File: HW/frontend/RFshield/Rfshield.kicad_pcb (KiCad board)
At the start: 4 copper layers, 73 x 50.9 mm, 432 parts, among them P1 CONN_01X01, P38 CLKIN, P39 CLKOUT, Q1 MOSFET_P, T1 RX_BALUN, T2 TX_BALUN, U1 MAX2837, U2 MAX5864, U3 SI5351C, X1 GSG-XTAL4PIN

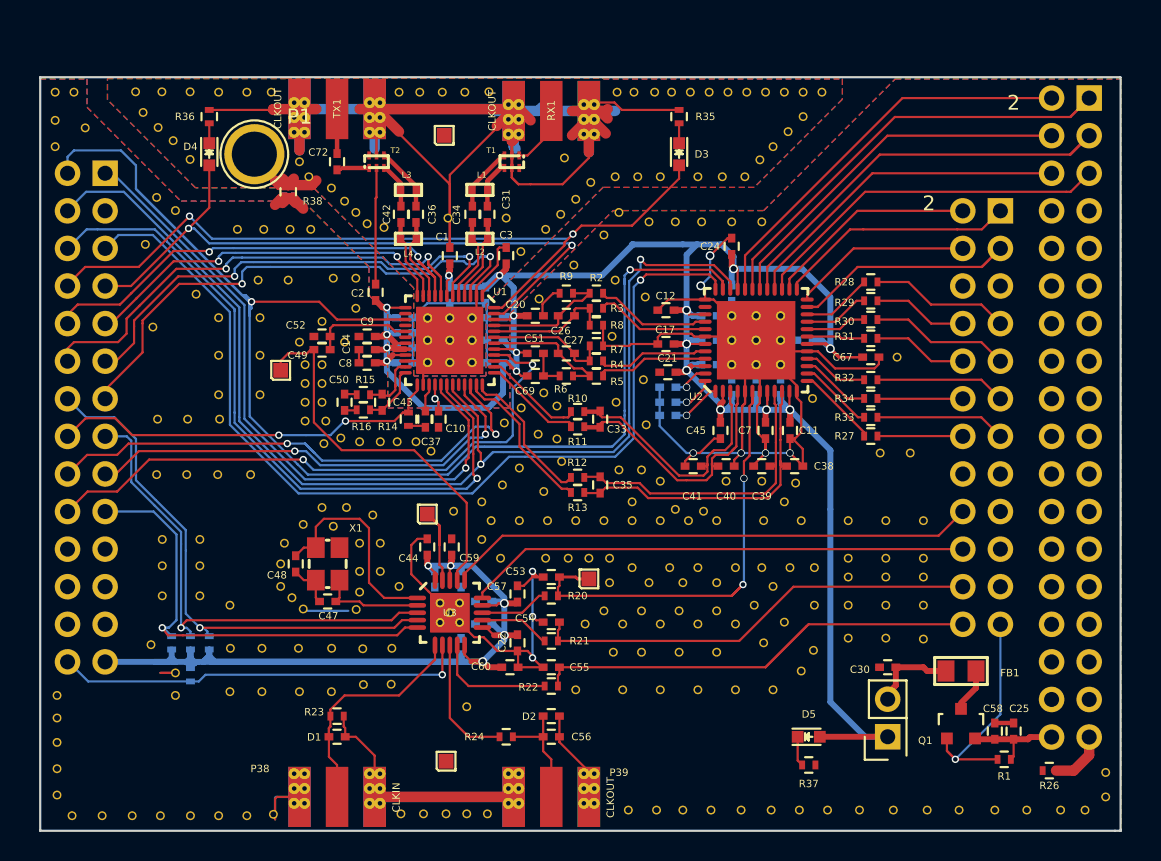
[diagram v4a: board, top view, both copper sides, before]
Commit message: Final text corrections
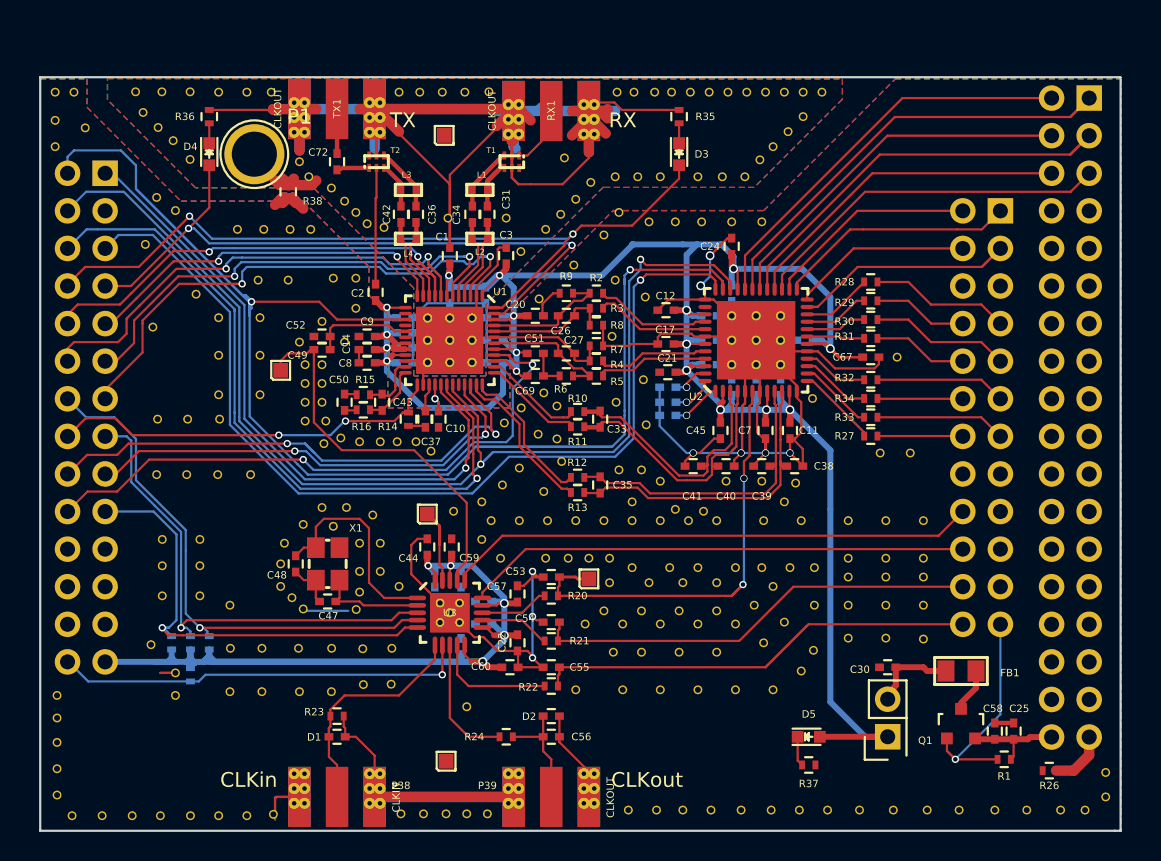
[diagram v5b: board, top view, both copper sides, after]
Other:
- board text added: "CLKin"
- board text added: "CLKout"
- board text added: "Quacho RF Shield v 1.0"
- board text added: "RX"
- board text added: "TX"
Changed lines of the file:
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@@
-(kicad_pcb (version 4) (host pcbnew 4.0.2-stable)
+(kicad_pcb (version 4) (host pcbnew 4.0.0-rc1-stable)
   (general
     (links 723)
     (no_connects 26)
-    (area 12.754 47.4758 123.009 132.4832)
+    (area 12.754 47.4758 122.5645 132.4832)
     (thickness 1.6)
-    (drawings 8)
+    (drawings 13)
     (tracks 1547)
     (zones 0)
@@
     (34 B.Paste user hide)
     (35 F.Paste user)
-    (36 B.SilkS user hide)
+    (36 B.SilkS user)
     (37 F.SilkS user)
     (38 B.Mask user hide)
@@
     (pad_to_mask_clearance 0)
     (aux_axis_origin 20 90)
-    (visible_elements 7FFECA3F)
+    (visible_elements 7FFEFFFF)
     (pcbplotparams
       (layerselection 0x010fc_80000001)
@@
   (module hackrf1:GSG-SMA-EDGE (layer F.Cu)
     (at 40.386 117.856 90)
-    (fp_text reference P38 (at 3.937 -5.207 180) (layer F.SilkS)
+    (fp_text reference P38 (at 2.794 4.318 180) (layer F.SilkS)
       (effects (font (size 0.50038 0.50038) (thickness 0.12446)))
     )
@@
   (module hackrf1:GSG-SMA-EDGE (layer F.Cu)
     (at 54.864 117.856 90)
-    (fp_text reference P39 (at 3.683 4.572 180) (layer F.SilkS)
+    (fp_text reference P39 (at 2.794 -4.318 180) (layer F.SilkS)
       (effects (font (size 0.50038 0.50038) (thickness 0.12446)))
     )
@@
       (net 94 0V_dig) (die_length -2147.483648))
   )
+  (gr_text TX (at 44.831 70.104) (layer F.SilkS)
+    (effects (font (size 1 1) (thickness 0.2)))
+  )
+  (gr_text RX (at 59.69 70.104) (layer F.SilkS)
+    (effects (font (size 1 1) (thickness 0.2)))
+  )
+  (gr_text CLKout (at 61.341 114.681) (layer F.SilkS)
+    (effects (font (size 1 1) (thickness 0.2)))
+  )
+  (gr_text CLKin (at 34.417 114.681) (layer F.SilkS)
+    (effects (font (size 1 1) (thickness 0.2)))
+  )
+  (gr_text "Quacho \nRF Shield\nv 1.0" (at 63.881 109.601) (layer B.SilkS)
+    (effects (font (size 2 2) (thickness 0.2)) (justify mirror))
+  )
   (gr_line (start 92.966 118.109) (end 93.336 118.109) (angle 90) (layer Edge.Cuts) (width 0.15))
   (gr_line (start 20.326 118.109) (end 92.966 118.109) (angle 90) (layer Edge.Cuts) (width 0.15))
@@
   (gr_line (start 20.326 67.209) (end 20.326 118.109) (angle 90) (layer Edge.Cuts) (width 0.15))
   (gr_line (start 20.316 67.189) (end 93.316 67.189) (angle 90) (layer Edge.Cuts) (width 0.15))
-  (gr_text 2 (at 86.103 68.919) (layer F.SilkS)
-    (effects (font (size 1 1) (thickness 0.25)))
+  (gr_text 2 (at 86.103 68.919) (layer B.SilkS)
+    (effects (font (size 1 1) (thickness 0.25)) (justify mirror))
   )
-  (gr_text 2 (at 80.383 75.719) (layer F.SilkS)
-    (effects (font (size 1 1) (thickness 0.25)))
+  (gr_text 2 (at 80.383 75.719) (layer B.SilkS)
+    (effects (font (size 1 1) (thickness 0.25)) (justify mirror))
   )
   (segment (start 91.213 88.919) (end 91.213 88.546) (width 0.15) (layer F.Cu) (net 0))
@@
   (segment (start 91.213 111.779) (end 91.213 113.003) (width 0.7) (layer F.Cu) (net 61))
   (segment (start 91.223 111.789) (end 91.213 111.779) (width 0.15) (layer F.Cu) (net 61))
-  (segment (start 85.213 104.159) (end 85.213 110.24) (width 0.15) (layer B.Cu) (net 62) (status 400000))
+  (segment (start 85.213 104.159) (end 85.213 110.24) (width 0.15) (layer B.Cu) (net 62))
   (segment (start 85.213 110.24) (end 82.169 113.284) (width 0.15) (layer B.Cu) (net 62))
   (segment (start 81.6 112.715) (end 82.169 113.284) (width 0.15) (layer F.Cu) (net 62))
@@
   (segment (start 44.45 79.502) (end 44.45 79.3115) (width 0.15) (layer F.Cu) (net 82))
   (segment (start 45.806 80.858) (end 44.45 79.502) (width 0.15) (layer F.Cu) (net 82))
-  (segment (start 36.576 86.995) (end 36.576 86.36) (width 0.15) (layer F.Cu) (net 83) (status 400000))
+  (segment (start 36.576 86.995) (end 36.576 86.36) (width 0.15) (layer F.Cu) (net 83))
   (segment (start 38.354 85.852) (end 37.084 85.852) (width 0.15) (layer F.Cu) (net 83))
   (segment (start 37.084 85.852) (end 36.576 86.36) (width 0.15) (layer F.Cu) (net 83))

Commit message: minor modifications
margin, vias and drc corrections
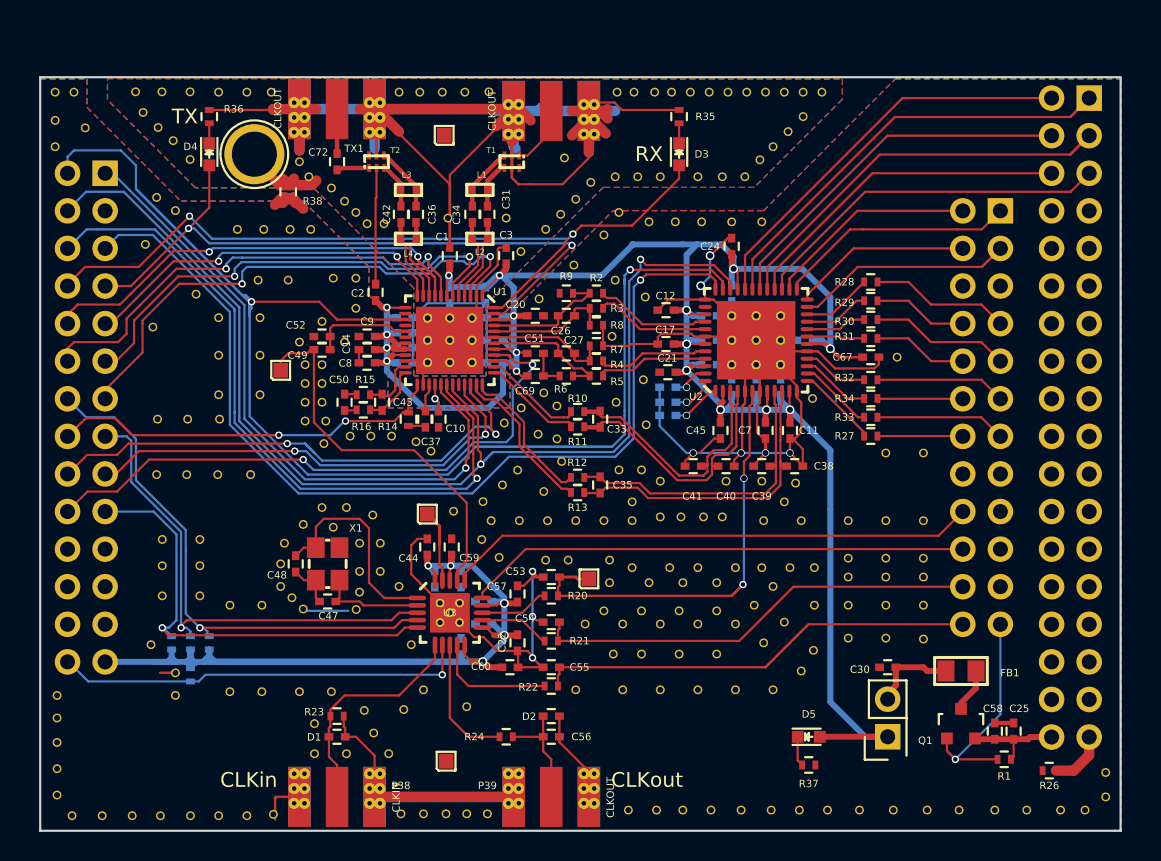
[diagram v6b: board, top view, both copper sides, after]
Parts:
- removed the ? at (64.1, 97.2)
- moved ? 18.2 mm to (42.2, 110.0)
- moved ? 16.2 mm to (44.9, 109.9)
- moved ? 8.10 mm to (43.9, 112.9)
- moved ? 7.63 mm to (38.9, 110.9)
- moved ? 7.20 mm to (38.9, 112.9)
- moved ? 5.74 mm to (42.9, 111.5)
- moved ? 4.81 mm to (41.0, 112.9)
- moved ? 2.91 mm to (35.3, 102.9)
- moved ? 2.22 mm to (46.2, 108.6)
- moved ? 1.34 mm to (45.4, 105.5)
- moved ? 0.89 mm to (80.0, 92.6)
- moved ? 0.85 mm to (42.7, 91.4)
- moved ? 0.65 mm to (41.3, 91.4)
- moved ? 0.63 mm to (63.6, 96.9)
- moved ? 0.54 mm to (44.1, 91.4)
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- renumbered RX1 to ?, P1 to ?
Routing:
- net GND: track 165.0 -> 169.5 mm
- net 0V_dig: track 194.3 -> 192.0 mm
